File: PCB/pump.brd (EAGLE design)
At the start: 97.8 x 100 mm, 16 parts, among them U1 ARDUINOR3-BPLACE, X1 HD44780LCD-1602

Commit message: Finished PCB
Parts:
- added JP14, JP15, JP16, JP17: (no value), adafruit:1X01
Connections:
- new net N$1: JP15.1, JP6.2
- new net N$6: JP4.1, U1.D3
- net N$5: now also JP17.1
- net VSS: now also JP14.1, JP16.1; no longer JP6.2
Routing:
- net N$1: track 0.00 -> 65.6 mm, vias 0 -> 2
- net N$6: track 0.00 -> 63.0 mm, vias 0 -> 1
- net N$5: track 144.8 -> 194.8 mm
- net VSS: track 271.3 -> 306.0 mm
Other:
- board text added: "47uF CAP"
- board text added: "ENC BYPASS"

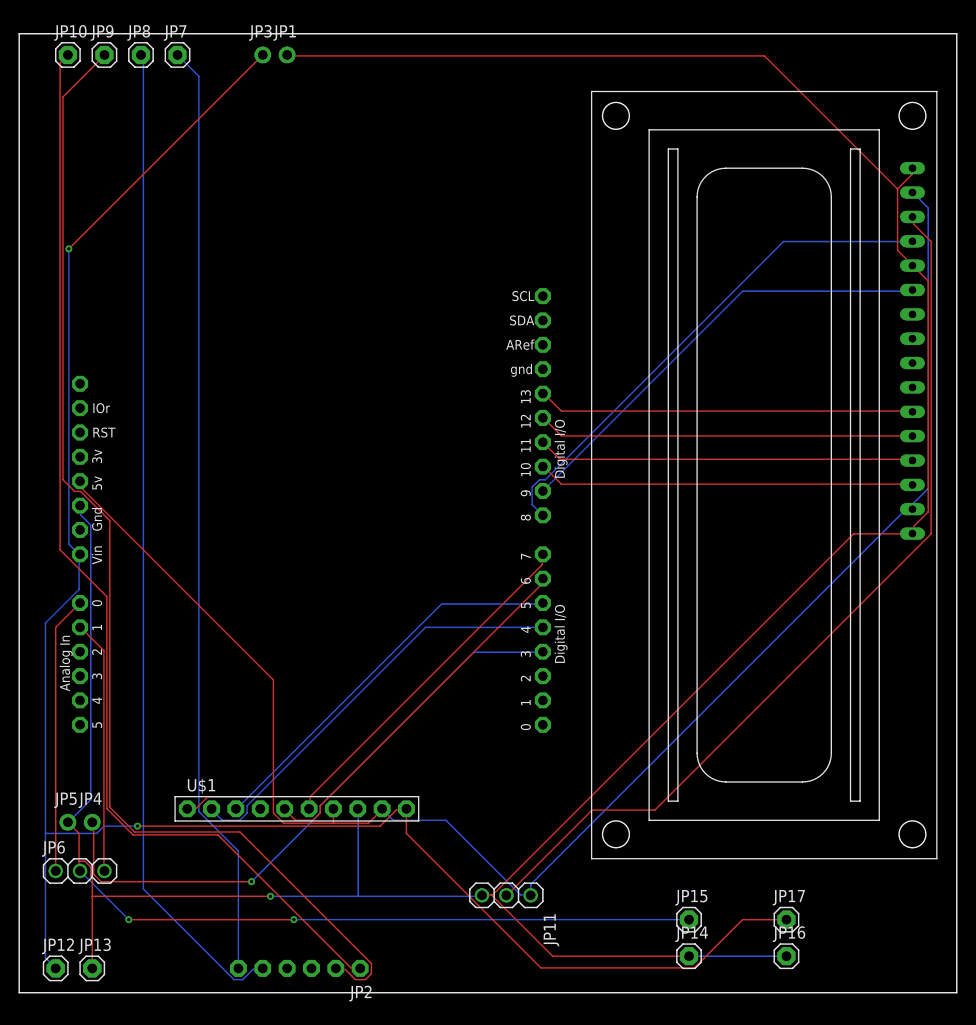
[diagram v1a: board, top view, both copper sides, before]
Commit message: Fixed driver spacing on PCB and rerouted traces
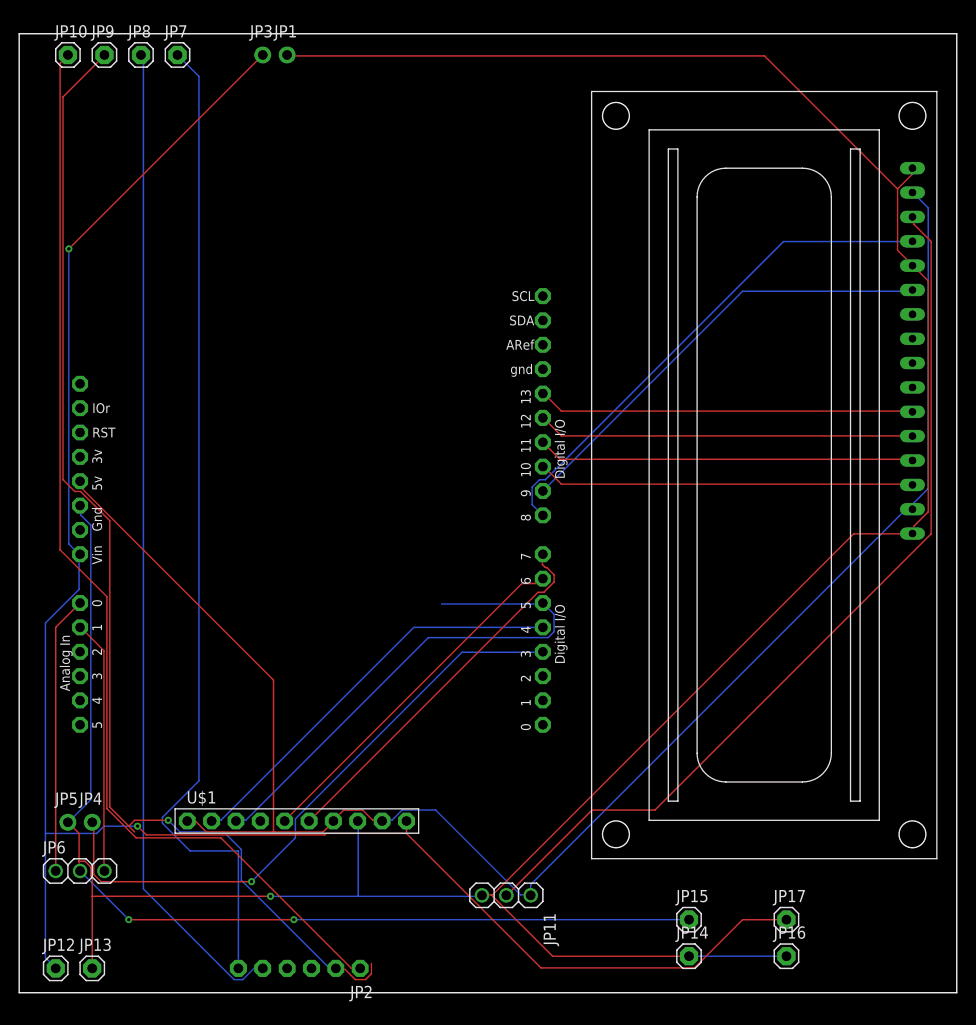
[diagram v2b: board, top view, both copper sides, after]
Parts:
- moved U$1 1.27 mm to (29.0, 17.9)
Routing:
- net N$20: track 40.9 -> 55.5 mm
- net N$22: track 97.9 -> 104.0 mm
- net N$18: track 36.7 -> 39.4 mm
- net N$5: track 194.8 -> 193.3 mm
- net VDD: track 177.3 -> 178.6 mm
- net VSS: track 306.0 -> 304.7 mm
- net N$21: track 43.9 -> 42.9 mm
- net N$6: track 63.0 -> 63.7 mm
- net N$24: track 122.2 -> 121.9 mm, vias 0 -> 1
